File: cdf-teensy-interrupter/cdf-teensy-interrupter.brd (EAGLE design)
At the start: 74.9 x 80 mm, 20 parts

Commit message: wip
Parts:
- added EMERGENCY: SWITCH-MOMENTARY-2PTH, SparkFun-Electromechanical:TACTILE-PTH
- added R7: 220, rcl:0204/7
- added SP1: SPEAKER/PS12, adafruit:PS12
- added T1: BC337, transistor:TO92
- moved LCD_BL 13.6 mm to (32.3, 59.9)
- moved D1 2.59 mm to (19.1, 42.7)
- moved R3 2.59 mm to (21.8, 54.9)
- moved OK1 2.59 mm to (27.9, 47.2)
- moved R1 2.59 mm to (18.3, 48.5)
- moved R2 2.59 mm to (22.4, 49.0)
- moved PULSE_WIDTH 1.27 mm to (25.1, 34.3)
- moved R5 1.02 mm to (16.8, 72.1)
- moved U$6 1.02 mm to (11.4, 78.5)
- moved PULSE_DUTY 1.02 mm to (8.89, 34.3)
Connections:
- new net EMERGENCY: EMERGENCY.1, U$2.11
- new net N$11: SP1.P$1, T1.3, U$6.P$1_CATHODE-
- new net N$7: R7.1, T1.2
- net +3V3: now also R3.2
- net +5V: now also R5.2, SP1.P$2; no longer R3.2
- net GND: now also EMERGENCY.3, T1.1; no longer U$6.P$1_CATHODE-
- net TX: now also R7.2; no longer R5.2
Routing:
- net EMERGENCY: track 0.00 -> 69.8 mm
- net +3V3: track 69.3 -> 100.5 mm
- net N$11: track 0.00 -> 27.1 mm
- net TX: track 47.4 -> 37.2 mm
- net N$7: track 0.00 -> 6.38 mm
- net N$5: track 54.3 -> 50.1 mm
- net N$1: track 6.43 -> 3.81 mm
- net RX: track 80.2 -> 77.9 mm
- net PULSE_WIDTH: track 20.7 -> 20.2 mm

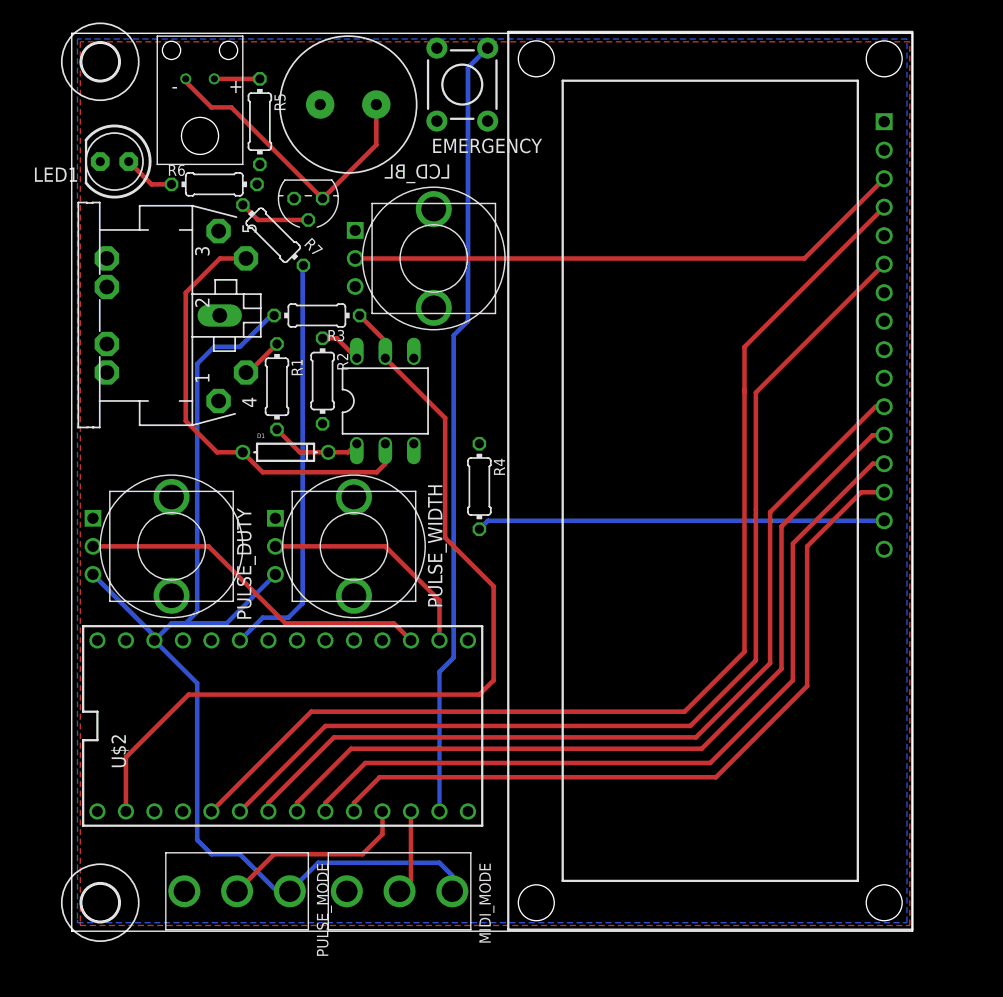
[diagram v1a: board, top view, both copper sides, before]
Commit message: add usb connector
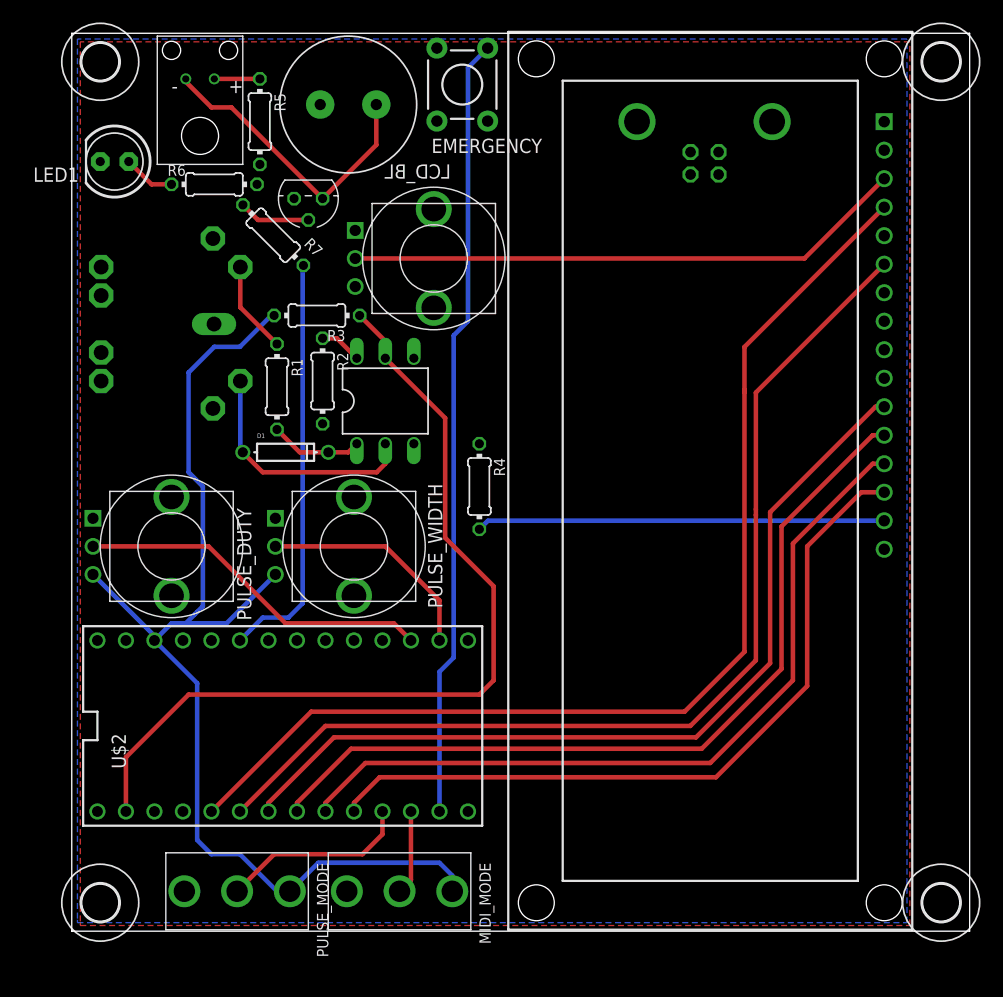
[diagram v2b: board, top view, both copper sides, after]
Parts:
- added H3, H4: MOUNT-HOLE3.3, holes:3,3
- added X1: (no value), keves:TE-292304-1
- moved U$1 0.92 mm to (0.00, 54.1), flipped to the bottom, turned to 90 degrees
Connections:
- net +5V: now also X1.1
- net GND: now also X1.4
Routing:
- net N$3: track 39.8 -> 22.0 mm
- net N$1: track 3.81 -> 8.21 mm
- net +3V3: track 100.5 -> 101.5 mm
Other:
- board size 74.9 x 80 mm -> 80 x 80 mm
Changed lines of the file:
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@@
 <?xml version="1.0" encoding="utf-8"?>
 <!DOCTYPE eagle SYSTEM "eagle.dtd">
-<eagle version="7.5.0">
+<eagle version="7.3.0">
 <drawing>
 <settings>
@@
 <layers>
 <layer number="1" name="Top" color="4" fill="1" visible="yes" active="yes"/>
+<layer number="2" name="Route2" color="1" fill="3" visible="yes" active="yes"/>
+<layer number="3" name="Route3" color="4" fill="3" visible="yes" active="yes"/>
+<layer number="4" name="Route4" color="1" fill="4" visible="yes" active="yes"/>
+<layer number="5" name="Route5" color="4" fill="4" visible="yes" active="yes"/>
+<layer number="6" name="Route6" color="1" fill="8" visible="yes" active="yes"/>
+<layer number="7" name="Route7" color="4" fill="8" visible="yes" active="yes"/>
+<layer number="8" name="Route8" color="1" fill="2" visible="yes" active="yes"/>
+<layer number="9" name="Route9" color="4" fill="2" visible="yes" active="yes"/>
+<layer number="10" name="Route10" color="1" fill="7" visible="yes" active="yes"/>
+<layer number="11" name="Route11" color="4" fill="7" visible="yes" active="yes"/>
+<layer number="12" name="Route12" color="1" fill="5" visible="yes" active="yes"/>
+<layer number="13" name="Route13" color="4" fill="5" visible="yes" active="yes"/>
+<layer number="14" name="Route14" color="1" fill="6" visible="yes" active="yes"/>
+<layer number="15" name="Route15" color="4" fill="6" visible="yes" active="yes"/>
 <layer number="16" name="Bottom" color="1" fill="1" visible="yes" active="yes"/>
 <layer number="17" name="Pads" color="2" fill="1" visible="yes" active="yes"/>
@@
 <layer number="56" name="wert" color="7" fill="1" visible="no" active="no"/>
 <layer number="57" name="tCAD" color="7" fill="1" visible="no" active="no"/>
+<layer number="58" name="bCAD" color="11" fill="1" visible="yes" active="yes"/>
 <layer number="59" name="tCarbon" color="7" fill="1" visible="no" active="no"/>
 <layer number="60" name="bCarbon" color="7" fill="1" visible="no" active="no"/>
@@
 <board>
 <plain>
-<wire x1="0" y1="0" x2="74.93" y2="0" width="0" layer="20"/>
-<wire x1="74.93" y1="0" x2="74.93" y2="80.01" width="0" layer="20"/>
-<wire x1="74.93" y1="80.01" x2="0" y2="80.01" width="0" layer="20"/>
+<wire x1="0" y1="0" x2="80.01" y2="0" width="0" layer="20"/>
+<wire x1="80.01" y1="0" x2="80.01" y2="80.01" width="0" layer="20"/>
+<wire x1="80.01" y1="80.01" x2="0" y2="80.01" width="0" layer="20"/>
 <wire x1="0" y1="80.01" x2="0" y2="0" width="0" layer="20"/>
 </plain>
@@
 <attribute name="VALUE" x="14.3256" y="67.0306" size="0.9906" layer="27" ratio="10" rot="R180"/>
 </element>
-<element name="U$1" library="keves" package="CP-2350" value="MIDIJACK" x="0.508" y="54.864" smashed="yes" rot="R270"/>
+<element name="U$1" library="keves" package="CP-2350" value="MIDIJACK" x="0" y="54.102" smashed="yes" rot="MR90"/>
 <element name="U$2" library="Teensy_3_and_LC_Series_Boards_v1.1" package="TEENSY3-DIL" value="TEENSY_3.1_DIL" x="18.796" y="18.288" smashed="yes" rot="R90">
 <attribute name="NAME" x="4.826" y="14.478" size="1.27" layer="25" font="vector" rot="R90"/>
@@
 <attribute name="VALUE" x="16.456115625" y="62.8278" size="0.9906" layer="27" ratio="10" rot="R315"/>
 </element>
+<element name="X1" library="keves" package="TE-292304-1" value="" x="56.388" y="72.136" rot="MR180">
+<attribute name="MPN" value="292304-1 " x="56.388" y="72.136" size="1.778" layer="28" rot="MR180" display="off"/>
+</element>
+<element name="H3" library="holes" package="3,3" value="MOUNT-HOLE3.3" x="77.47" y="2.54"/>
+<element name="H4" library="holes" package="3,3" value="MOUNT-HOLE3.3" x="77.47" y="77.47"/>
 </elements>
 <signals>
@@
 <contactref element="U$1" pad="4"/>
 <contactref element="R1" pad="1"/>
-<wire x1="15.528" y1="49.784" x2="15.748" y2="49.784" width="0.4064" layer="1"/>
-<wire x1="15.748" y1="49.784" x2="18.288" y2="52.324" width="0.4064" layer="1"/>
+<wire x1="15.02" y1="59.182" x2="15.02" y2="55.592" width="0.4064" layer="1"/>
+<wire x1="15.02" y1="55.592" x2="18.288" y2="52.324" width="0.4064" layer="1"/>
 </signal>
 <signal name="N$2">
@@
 <wire x1="27.178" y1="40.894" x2="17.018" y2="40.894" width="0.4064" layer="1"/>
 <wire x1="17.018" y1="40.894" x2="15.24" y2="42.672" width="0.4064" layer="1"/>
-<wire x1="15.528" y1="59.944" x2="13.208" y2="59.944" width="0.4064" layer="1"/>
-<wire x1="13.208" y1="59.944" x2="10.16" y2="56.896" width="0.4064" layer="1"/>
-<wire x1="10.16" y1="56.896" x2="10.16" y2="45.466" width="0.4064" layer="1"/>
-<wire x1="10.16" y1="45.466" x2="12.954" y2="42.672" width="0.4064" layer="1"/>
-<wire x1="12.954" y1="42.672" x2="15.24" y2="42.672" width="0.4064" layer="1"/>
+<wire x1="15.02" y1="49.022" x2="15.02" y2="42.892" width="0.4064" layer="16"/>
+<wire x1="15.02" y1="42.892" x2="15.24" y2="42.672" width="0.4064" layer="16"/>
 </signal>
 <signal name="GND">
@@
 <contactref element="EMERGENCY" pad="3"/>
 <contactref element="T1" pad="1"/>
+<contactref element="X1" pad="4"/>
 </signal>
 <signal name="+5V">
@@
 <contactref element="SP1" pad="P$2"/>
 <contactref element="R5" pad="2"/>
+<contactref element="X1" pad="1"/>
 </signal>
 <signal name="N$4">
@@
 <wire x1="17.78" y1="54.864" x2="14.986" y2="52.07" width="0.4064" layer="16"/>
 <wire x1="14.986" y1="52.07" x2="12.7" y2="52.07" width="0.4064" layer="16"/>
-<wire x1="12.7" y1="52.07" x2="11.176" y2="50.546" width="0.4064" layer="16"/>
-<wire x1="11.176" y1="50.546" x2="11.176" y2="28.448" width="0.4064" layer="16"/>
-<wire x1="11.176" y1="28.448" x2="10.16" y2="27.432" width="0.4064" layer="16"/>
+<wire x1="12.7" y1="52.07" x2="10.414" y2="49.784" width="0.4064" layer="16"/>
+<wire x1="11.176" y1="28.448" x2="10.922" y2="28.194" width="0.4064" layer="16"/>
+<wire x1="10.922" y1="28.194" x2="10.16" y2="27.432" width="0.4064" layer="16"/>
+<wire x1="10.414" y1="49.784" x2="10.414" y2="40.894" width="0.4064" layer="16"/>
+<wire x1="10.414" y1="40.894" x2="11.684" y2="39.624" width="0.4064" layer="16"/>
+<wire x1="11.684" y1="39.624" x2="11.684" y2="28.956" width="0.4064" layer="16"/>
+<wire x1="11.684" y1="28.956" x2="11.176" y2="28.448" width="0.4064" layer="16"/>
 </signal>
 <signal name="LCD_EN">

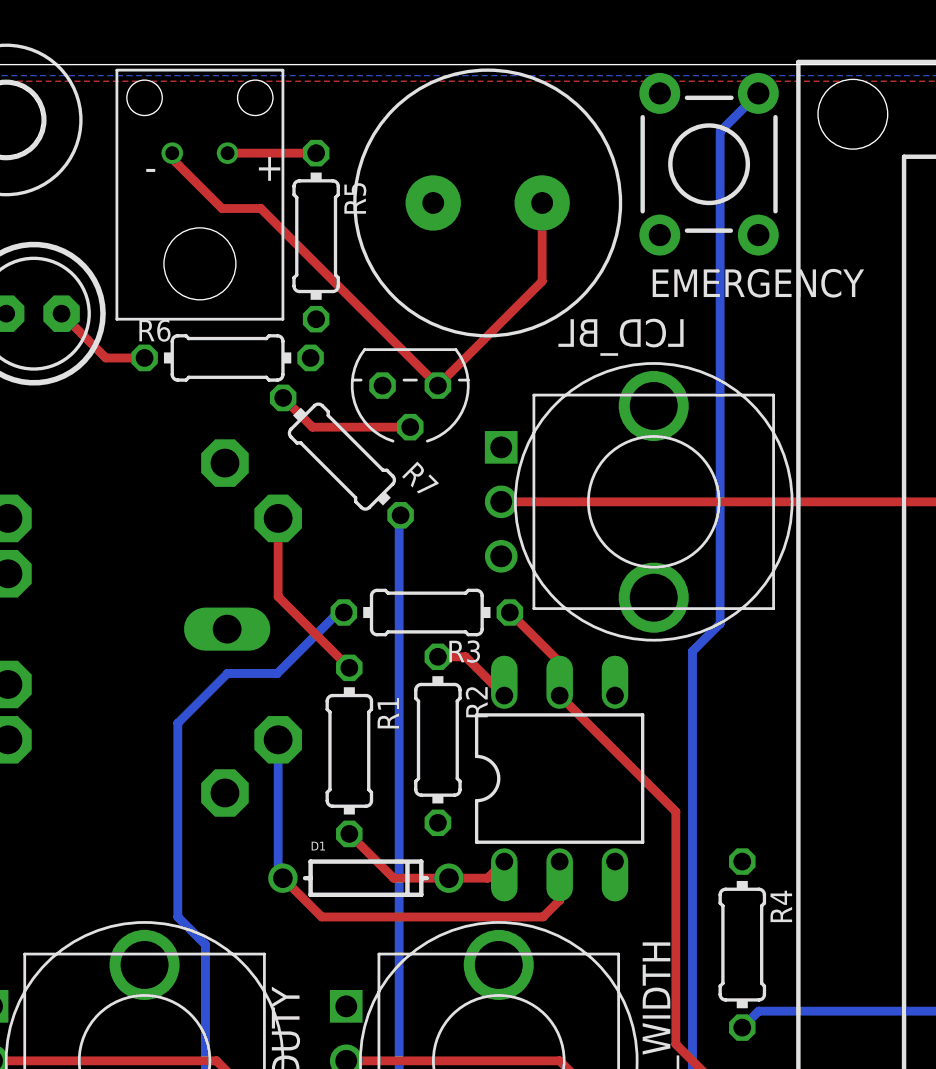
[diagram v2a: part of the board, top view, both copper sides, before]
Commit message: correct optical footprint
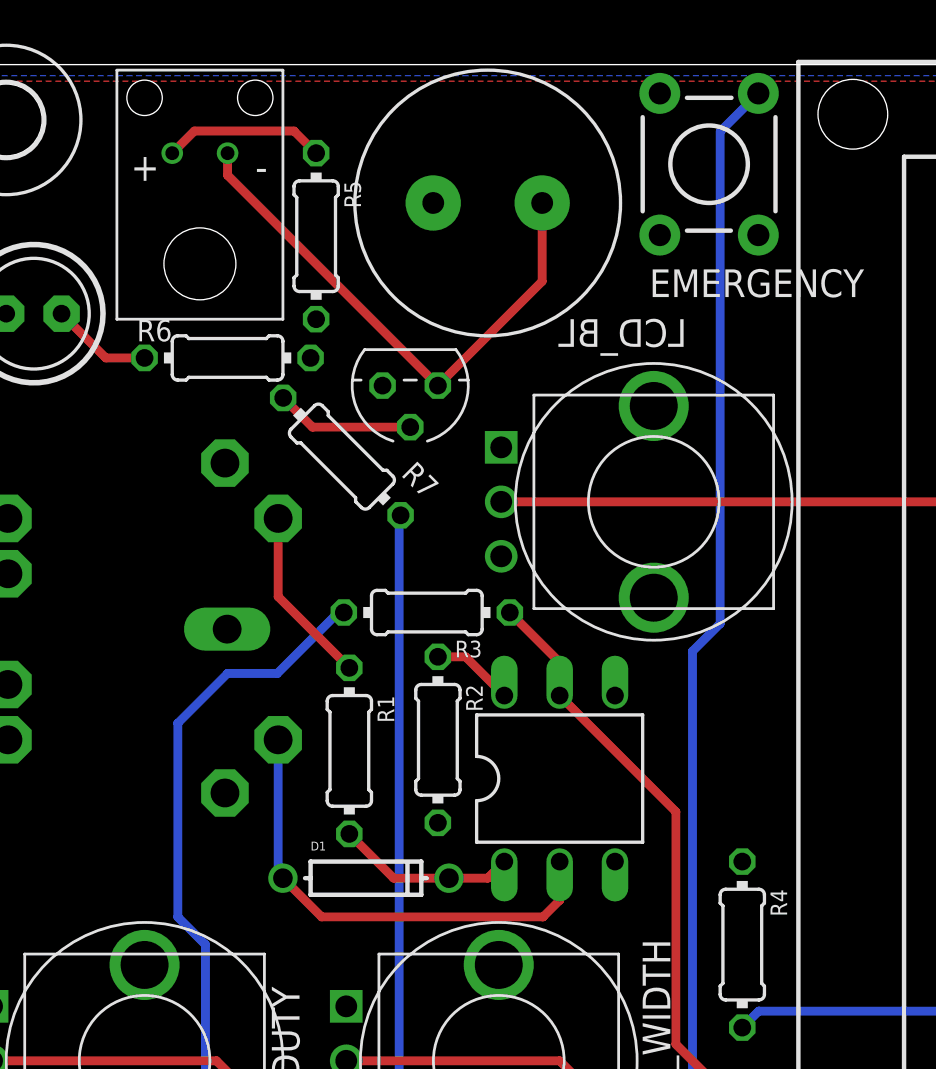
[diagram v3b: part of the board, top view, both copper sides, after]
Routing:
- net N$8: track 4.06 -> 7.45 mm
- net N$11: track 27.1 -> 25.0 mm
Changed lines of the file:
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@@
 <layers>
 <layer number="1" name="Top" color="4" fill="1" visible="yes" active="yes"/>
-<layer number="2" name="Route2" color="1" fill="3" visible="yes" active="yes"/>
-<layer number="3" name="Route3" color="4" fill="3" visible="yes" active="yes"/>
-<layer number="4" name="Route4" color="1" fill="4" visible="yes" active="yes"/>
-<layer number="5" name="Route5" color="4" fill="4" visible="yes" active="yes"/>
-<layer number="6" name="Route6" color="1" fill="8" visible="yes" active="yes"/>
-<layer number="7" name="Route7" color="4" fill="8" visible="yes" active="yes"/>
-<layer number="8" name="Route8" color="1" fill="2" visible="yes" active="yes"/>
-<layer number="9" name="Route9" color="4" fill="2" visible="yes" active="yes"/>
-<layer number="10" name="Route10" color="1" fill="7" visible="yes" active="yes"/>
-<layer number="11" name="Route11" color="4" fill="7" visible="yes" active="yes"/>
-<layer number="12" name="Route12" color="1" fill="5" visible="yes" active="yes"/>
-<layer number="13" name="Route13" color="4" fill="5" visible="yes" active="yes"/>
-<layer number="14" name="Route14" color="1" fill="6" visible="yes" active="yes"/>
-<layer number="15" name="Route15" color="4" fill="6" visible="yes" active="yes"/>
 <layer number="16" name="Bottom" color="1" fill="1" visible="yes" active="yes"/>
 <layer number="17" name="Pads" color="2" fill="1" visible="yes" active="yes"/>
@@
 <contactref element="R5" pad="1"/>
 <contactref element="U$6" pad="P$2_ANODE+"/>
-<wire x1="12.7" y1="75.946" x2="16.764" y2="75.946" width="0.4064" layer="1"/>
+<wire x1="16.764" y1="75.946" x2="15.748" y2="76.962" width="0.4064" layer="1"/>
+<wire x1="15.748" y1="76.962" x2="11.176" y2="76.962" width="0.4064" layer="1"/>
+<wire x1="11.176" y1="76.962" x2="10.16" y2="75.946" width="0.4064" layer="1"/>
 </signal>
 <signal name="N$9">
@@
 <wire x1="27.138" y1="73.66" x2="27.138" y2="70.064" width="0.4064" layer="1"/>
 <wire x1="27.138" y1="70.064" x2="22.352" y2="65.278" width="0.4064" layer="1"/>
-<wire x1="10.16" y1="75.946" x2="10.16" y2="75.692" width="0.4064" layer="1"/>
-<wire x1="10.16" y1="75.692" x2="12.446" y2="73.406" width="0.4064" layer="1"/>
-<wire x1="12.446" y1="73.406" x2="14.224" y2="73.406" width="0.4064" layer="1"/>
-<wire x1="14.224" y1="73.406" x2="22.352" y2="65.278" width="0.4064" layer="1"/>
+<wire x1="12.7" y1="74.93" x2="22.352" y2="65.278" width="0.4064" layer="1"/>
+<wire x1="12.7" y1="75.946" x2="12.7" y2="74.93" width="0.4064" layer="1"/>
 </signal>
 </signals>
